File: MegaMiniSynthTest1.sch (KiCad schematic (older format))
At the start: 35 parts, among them K1 CONN_3, P4 DIN_5, U1 MC33269, U2 TLE2426, U3 PCA9685

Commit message: Moved to new KiCad Version
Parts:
- removed E1: RGBROTARYENCODER, MODULE, symbol RGBROTARYENCODER
- added E1: RGBRotaryEncoder, MODULE, symbol RGBRotaryEncoder
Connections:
- wire segments 107 -> 106
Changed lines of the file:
@@
-EESchema Schematic File Version 2  date Saturday, 16 August 2014 10:36:46
+EESchema Schematic File Version 2
 LIBS:power
 LIBS:device
@@
 LIBS:led_rgb
 LIBS:MegaMiniSynthTest1-cache
-EELAYER 27 0
+EELAYER 24 0
 EELAYER END
 $Descr A4 11693 8268
@@
 Sheet 1 1
 Title "MegaMiniSynth Test 1"
-Date "15 aug 2014"
+Date "16 aug 2014"
 Rev "1.0"
 Comp "Quentin McDonald"
@@
 $EndComp
 $Comp
-L RGBROTARYENCODER E1
-U 1 1 53EC01C1
-P 9400 4900
-F 0 "E1" H 9400 4800 50  0000 C CNN
-F 1 "RGBROTARYENCODER" H 9400 5150 50  0000 C CNN
-F 2 "MODULE" H 9400 4900 50  0001 C CNN
-F 3 "DOCUMENTATION" H 9400 4900 50  0001 C CNN
-	1    9400 4900
-	1    0    0    -1
-$EndComp
-$Comp
 L GND #PWR019
 U 1 1 53EC01F3
@@
 	8400 4750 8400 4500
 Wire Wire Line
-	7900 5600 7900 5200
-Wire Wire Line
-	7250 5600 7900 5600
-Wire Wire Line
-	7900 4850 7800 4850
-Wire Wire Line
-	7800 4850 7800 5500
-Wire Wire Line
-	7800 5500 7250 5500
-Wire Wire Line
-	7700 4500 7900 4500
-Wire Wire Line
-	7700 5400 7700 4500
-Wire Wire Line
-	7250 5400 7700 5400
-Wire Wire Line
 	8650 4950 8500 4950
 Wire Wire Line
@@
 Wire Wire Line
 	4700 5100 5000 5100
-Wire Wire Line
-	5750 5500 5500 5500
-Wire Wire Line
-	5500 5300 5600 5300
-Wire Wire Line
-	5600 5300 5600 5400
-Wire Wire Line
-	5600 5400 5750 5400
-Wire Wire Line
-	5500 5100 5650 5100
-Wire Wire Line
-	5650 5100 5650 5300
-Wire Wire Line
-	5650 5300 5750 5300
 Wire Wire Line
 	9400 2900 9050 2900
@@
 	0    1    1    0
 $EndComp
+Wire Wire Line
+	7900 5200 7450 5200
+Wire Wire Line
+	7450 5200 7450 5400
+Wire Wire Line
+	7450 5400 7250 5400
+Wire Wire Line
+	7900 4850 7550 4850
+Wire Wire Line
+	7550 4850 7550 5500
+Wire Wire Line
+	7550 5500 7250 5500
+Wire Wire Line
+	7900 4500 7750 4500
+Wire Wire Line
+	7750 4500 7750 5600
+Wire Wire Line
+	7750 5600 7250 5600
+Wire Wire Line
+	5500 5300 5750 5300
+Wire Wire Line
+	5500 5100 5600 5100
+Wire Wire Line
+	5600 5100 5600 5400
+Wire Wire Line
+	5600 5400 5750 5400
+Wire Wire Line
+	5500 5500 5750 5500
+$Comp
+L RGBRotaryEncoder E1
+U 1 1 53EEFE8B
+P 9400 4900
+F 0 "E1" H 9400 4800 50  0000 C CNN
+F 1 "RGBRotaryEncoder" H 9400 5150 50  0000 C CNN
+F 2 "MODULE" H 9400 4900 50  0001 C CNN
+F 3 "DOCUMENTATION" H 9400 4900 50  0001 C CNN
+	1    9400 4900
+	1    0    0    -1
+$EndComp
 $EndSCHEMATC

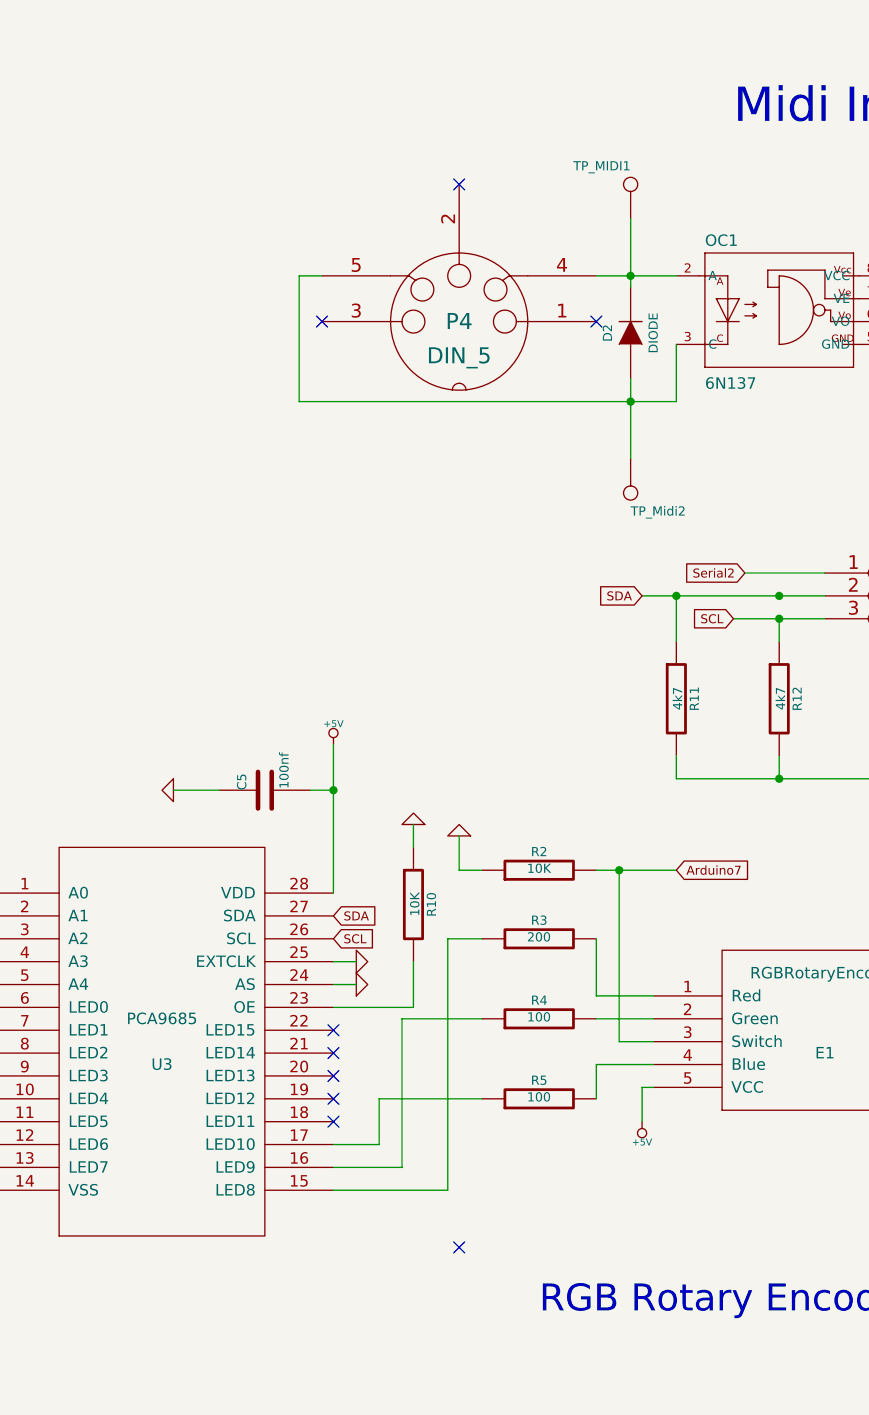
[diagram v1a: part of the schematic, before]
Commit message: Added missing resistor for MIDI in
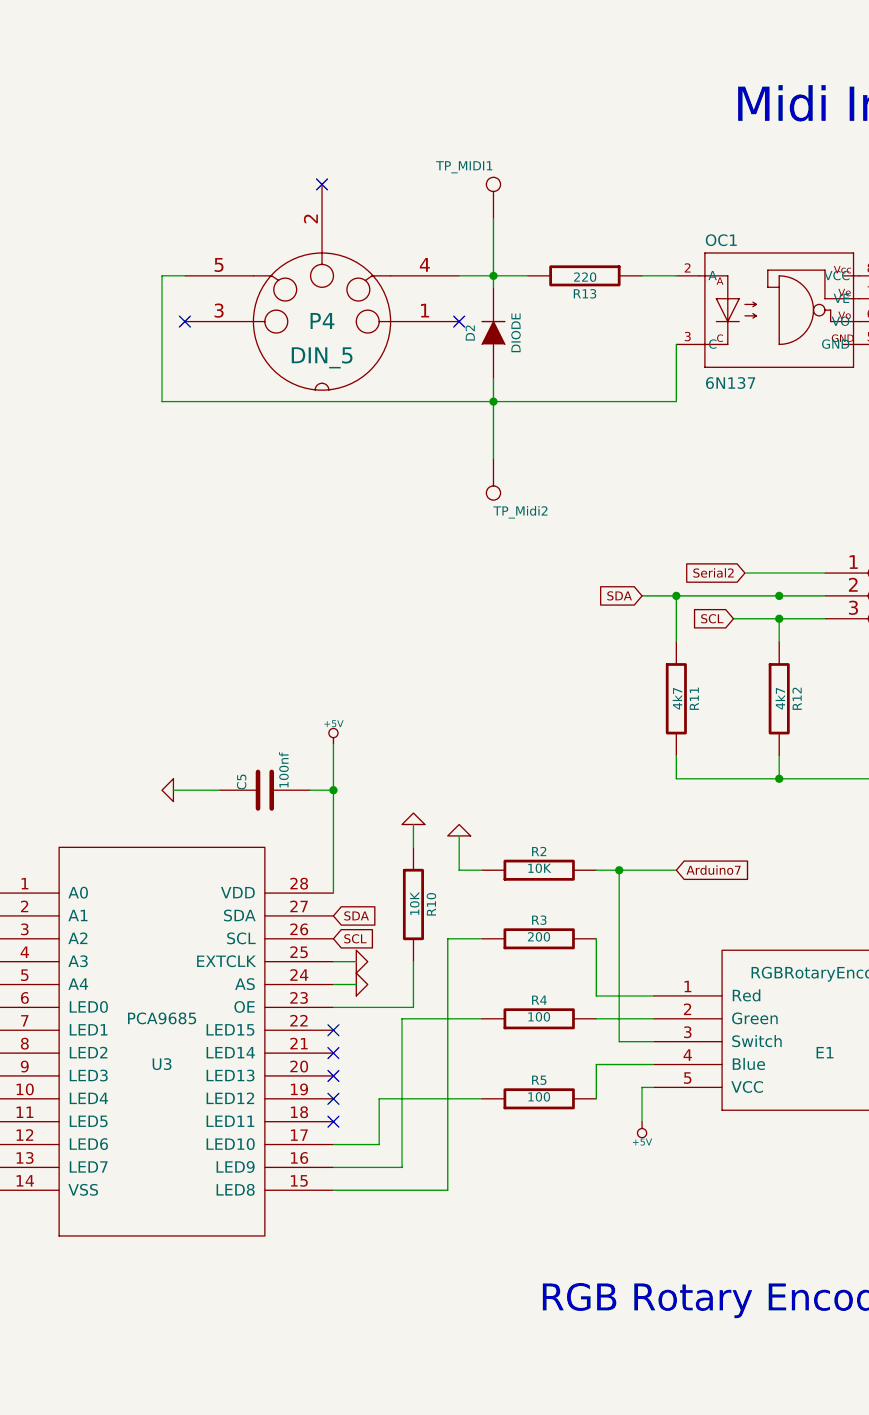
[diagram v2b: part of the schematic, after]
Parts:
- added R13: 220, symbol R
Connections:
- net at D2.2 (K), P4.4, TP_MIDI1.1: now also R13.2; no longer OC1.2 (A)
- new net: OC1.2 (A), R13.1
- no-connect marks 36 -> 35
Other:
- moved on the sheet: D2, P4, TP_MIDI1, TP_Midi2
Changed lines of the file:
@@
 L DIODE D2
 U 1 1 53EBFAE8
-P 8550 1850
-F 0 "D2" H 8550 1950 40  0000 C CNN
-F 1 "DIODE" H 8550 1750 40  0000 C CNN
-F 2 "~" H 8550 1850 60  0000 C CNN
-F 3 "~" H 8550 1850 60  0000 C CNN
-	1    8550 1850
+P 7950 1850
+F 0 "D2" H 7950 1950 40  0000 C CNN
+F 1 "DIODE" H 7950 1750 40  0000 C CNN
+F 2 "~" H 7950 1850 60  0000 C CNN
+F 3 "~" H 7950 1850 60  0000 C CNN
+	1    7950 1850
 	0    -1   -1   0
 $EndComp
@@
 	0    -1   -1   0
 $EndComp
-NoConn ~ 8400 1800
-NoConn ~ 7200 1800
+NoConn ~ 7800 1800
+NoConn ~ 6600 1800
 Text Notes 9000 950  0    150  ~ 0
 Midi In
@@
 NoConn ~ 7250 5000
 NoConn ~ 7250 4900
-NoConn ~ 7800 5850
 $Comp
 L GND #PWR022
@@
 	500  2950 500  500
 Wire Wire Line
-	8400 1600 8750 1600
-Wire Wire Line
-	7200 1600 7100 1600
-Wire Wire Line
-	7100 1600 7100 2150
-Wire Wire Line
-	7100 2150 8750 2150
+	6600 1600 6500 1600
+Wire Wire Line
+	6500 1600 6500 2150
+Wire Wire Line
+	6500 2150 8750 2150
 Wire Wire Line
 	8750 2150 8750 1900
-Connection ~ 8550 2150
-Connection ~ 8550 1600
+Connection ~ 7950 2150
+Connection ~ 7950 1600
 Wire Wire Line
 	9850 1700 9650 1700
@@
 	5450 5600 5450 5800
 Wire Wire Line
-	7250 4300 7250 3650
+	7250 3650 7250 4300
 Wire Wire Line
 	7250 4600 7350 4600
@@
 Text GLabel 8600 3000 0    39   Input ~ 0
 SDA
-NoConn ~ 7800 1200
+NoConn ~ 7200 1200
 $Comp
 L DIN_5 P4
 U 1 1 53EBFA7A
-P 7800 1800
-F 0 "P4" H 7800 1800 70  0000 C CNN
-F 1 "DIN_5" H 7800 1650 70  0000 C CNN
-F 2 "~" H 7800 1800 60  0000 C CNN
-F 3 "~" H 7800 1800 60  0000 C CNN
-	1    7800 1800
+P 7200 1800
+F 0 "P4" H 7200 1800 70  0000 C CNN
+F 1 "DIN_5" H 7200 1650 70  0000 C CNN
+F 2 "~" H 7200 1800 60  0000 C CNN
+F 3 "~" H 7200 1800 60  0000 C CNN
+	1    7200 1800
 	1    0    0    -1
 $EndComp
@@
 L CONN_1 TP_MIDI1
 U 1 1 53EC5C52
-P 8550 1200
-F 0 "TP_MIDI1" V 8630 1200 40  0000 L CNN
-F 1 "CONN_1" H 8550 1255 30  0001 C CNN
-F 2 "~" H 8550 1200 60  0000 C CNN
-F 3 "~" H 8550 1200 60  0000 C CNN
-	1    8550 1200
-	0    -1   -1   0
-$EndComp
-Wire Wire Line
-	8550 1350 8550 1650
+P 7950 1200
+F 0 "TP_MIDI1" V 8030 1200 40  0000 L CNN
+F 1 "CONN_1" H 7950 1255 30  0001 C CNN
+F 2 "~" H 7950 1200 60  0000 C CNN
+F 3 "~" H 7950 1200 60  0000 C CNN
+	1    7950 1200
+	0    -1   -1   0
+$EndComp
+Wire Wire Line
+	7950 1350 7950 1650
 $Comp
 L CONN_1 TP_Midi2
 U 1 1 53EC5DAA
-P 8550 2550
-F 0 "TP_Midi2" V 8630 2550 40  0000 L CNN
-F 1 "CONN_1" H 8550 2605 30  0001 C CNN
-F 2 "~" H 8550 2550 60  0000 C CNN
-F 3 "~" H 8550 2550 60  0000 C CNN
-	1    8550 2550
+P 7950 2550
+F 0 "TP_Midi2" V 8030 2550 40  0000 L CNN
+F 1 "CONN_1" H 7950 2605 30  0001 C CNN
+F 2 "~" H 7950 2550 60  0000 C CNN
+F 3 "~" H 7950 2550 60  0000 C CNN
+	1    7950 2550
 	0    1    1    0
 $EndComp
 Wire Wire Line
-	8550 2050 8550 2400
+	7950 2050 7950 2400
 $Comp
 L CONN_1 TP_MidiOut1
@@
 	1    0    0    -1
 $EndComp
+$Comp
+L R R13
+U 1 1 540F93B7
+P 8350 1600
+F 0 "R13" V 8430 1600 40  0000 C CNN
+F 1 "220" V 8357 1601 40  0000 C CNN
+F 2 "" V 8280 1600 30  0000 C CNN
+F 3 "" H 8350 1600 30  0000 C CNN
+	1    8350 1600
+	0    1    1    0
+$EndComp
+Wire Wire Line
+	7800 1600 8100 1600
+Wire Wire Line
+	8600 1600 8750 1600
 $EndSCHEMATC

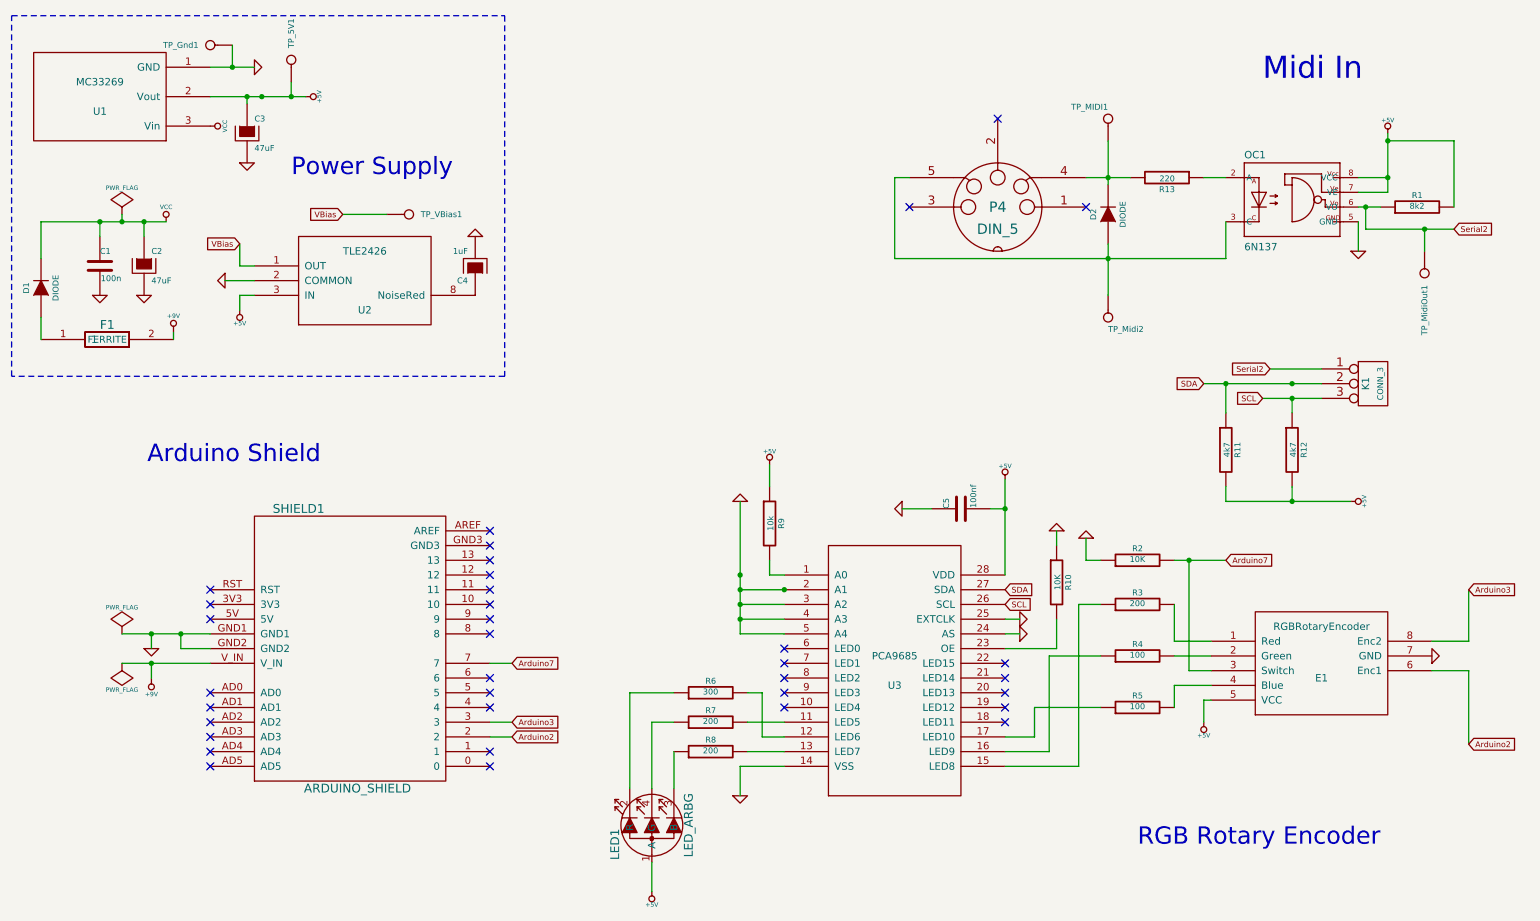
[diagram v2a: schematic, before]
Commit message: Changed some resistor values
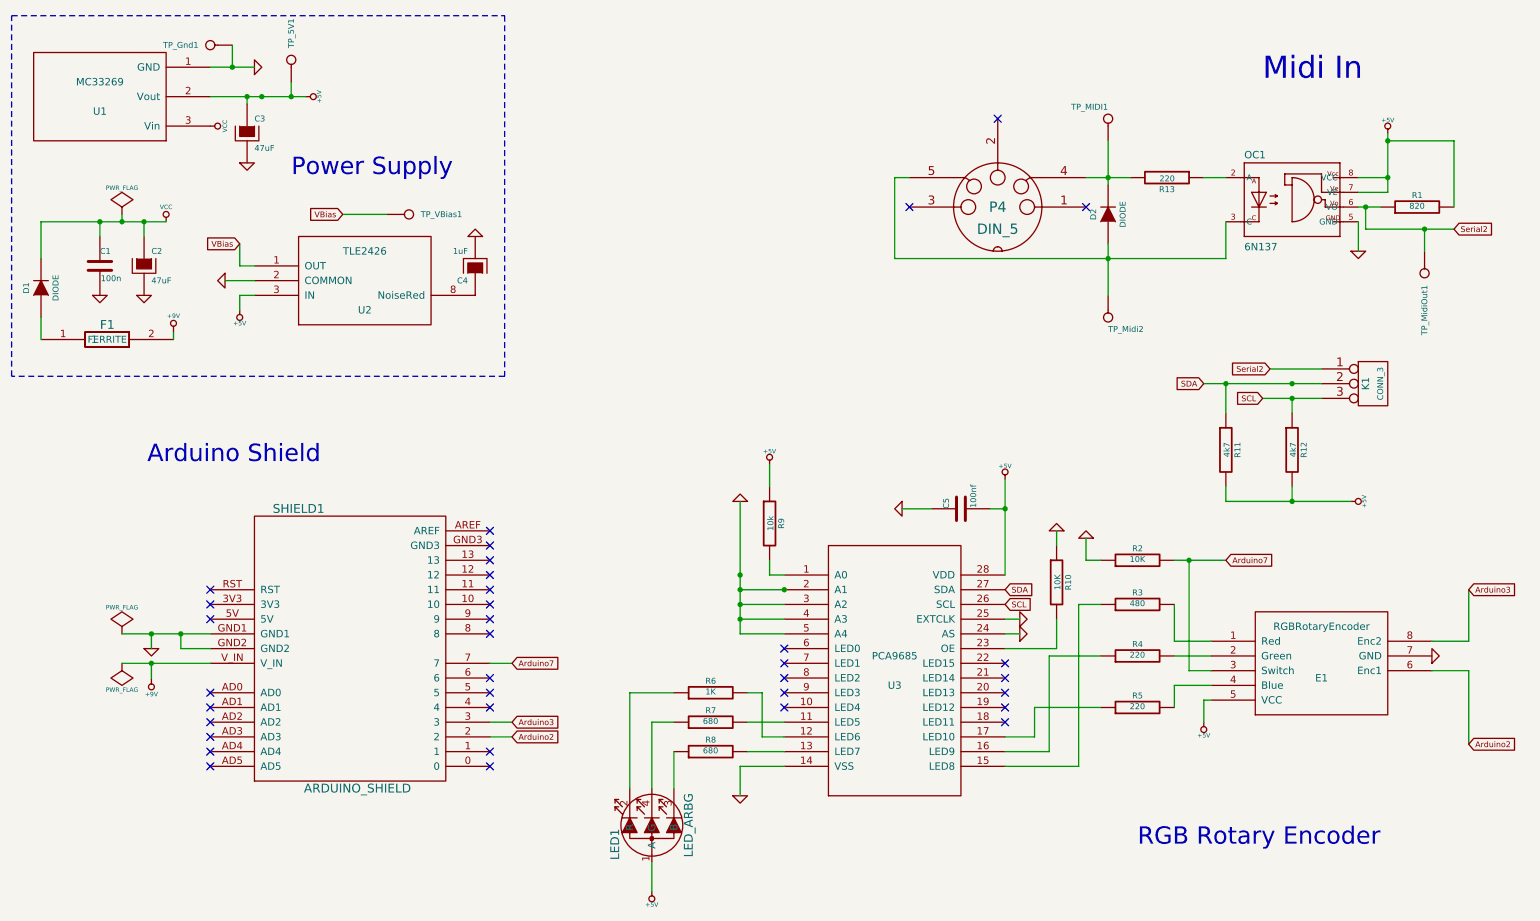
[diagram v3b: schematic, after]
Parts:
- R1: value 8k2 -> 820
- R3: value 200 -> 480
- R4, R5: value 100 -> 220
- R6: value 300 -> 1K
- R7, R8: value 200 -> 680
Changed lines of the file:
@@
 P 10050 1800
 F 0 "R1" V 10130 1800 40  0000 C CNN
-F 1 "8k2" V 10057 1801 40  0000 C CNN
+F 1 "820" V 10057 1801 40  0000 C CNN
 F 2 "~" V 9980 1800 30  0000 C CNN
 F 3 "~" H 10050 1800 30  0000 C CNN
@@
 P 8150 5200
 F 0 "R5" V 8230 5200 40  0000 C CNN
-F 1 "100" V 8157 5201 40  0000 C CNN
+F 1 "220" V 8157 5201 40  0000 C CNN
 F 2 "~" V 8080 5200 30  0000 C CNN
 F 3 "~" H 8150 5200 30  0000 C CNN
@@
 P 8150 4850
 F 0 "R4" V 8230 4850 40  0000 C CNN
-F 1 "100" V 8157 4851 40  0000 C CNN
+F 1 "220" V 8157 4851 40  0000 C CNN
 F 2 "~" V 8080 4850 30  0000 C CNN
 F 3 "~" H 8150 4850 30  0000 C CNN
@@
 P 8150 4500
 F 0 "R3" V 8230 4500 40  0000 C CNN
-F 1 "200" V 8157 4501 40  0000 C CNN
+F 1 "480" V 8157 4501 40  0000 C CNN
 F 2 "~" V 8080 4500 30  0000 C CNN
 F 3 "~" H 8150 4500 30  0000 C CNN
@@
 P 5250 5500
 F 0 "R8" V 5330 5500 40  0000 C CNN
-F 1 "200" V 5257 5501 40  0000 C CNN
+F 1 "680" V 5257 5501 40  0000 C CNN
 F 2 "~" V 5180 5500 30  0000 C CNN
 F 3 "~" H 5250 5500 30  0000 C CNN
@@
 P 5250 5300
 F 0 "R7" V 5330 5300 40  0000 C CNN
-F 1 "200" V 5257 5301 40  0000 C CNN
+F 1 "680" V 5257 5301 40  0000 C CNN
 F 2 "~" V 5180 5300 30  0000 C CNN
 F 3 "~" H 5250 5300 30  0000 C CNN
@@
 P 5250 5100
 F 0 "R6" V 5330 5100 40  0000 C CNN
-F 1 "300" V 5257 5101 40  0000 C CNN
+F 1 "1K" V 5257 5101 40  0000 C CNN
 F 2 "~" V 5180 5100 30  0000 C CNN
 F 3 "~" H 5250 5100 30  0000 C CNN
